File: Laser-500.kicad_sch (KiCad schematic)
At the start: 0 parts

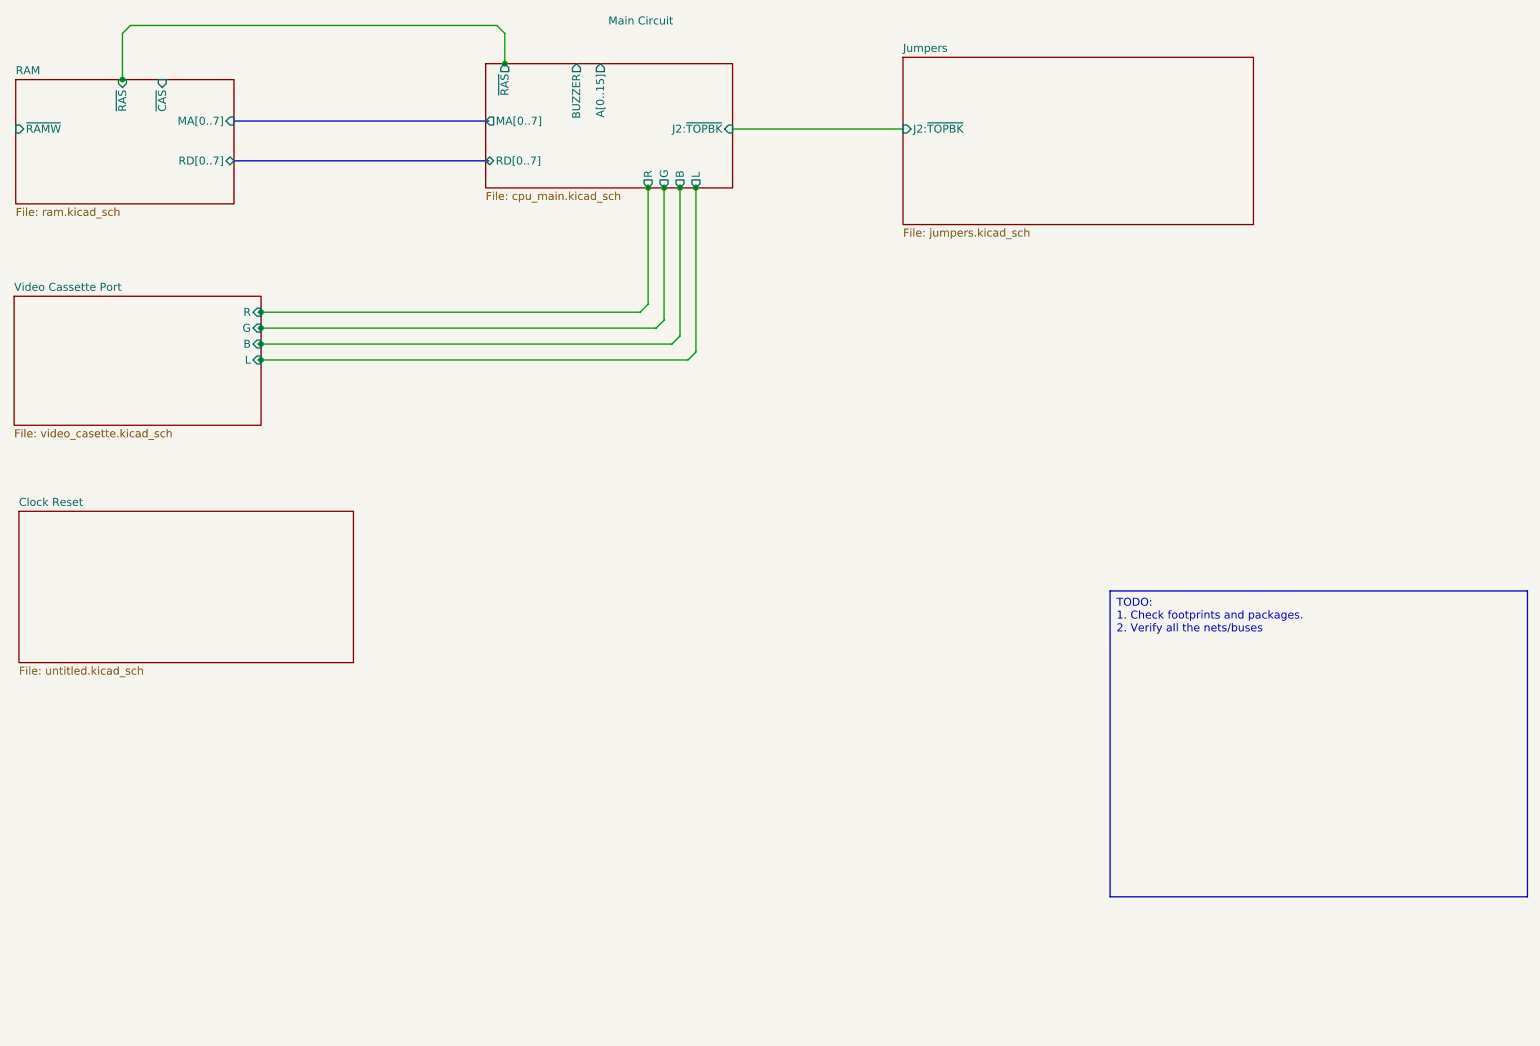
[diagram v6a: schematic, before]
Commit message: More updates on Top and Main diagrams
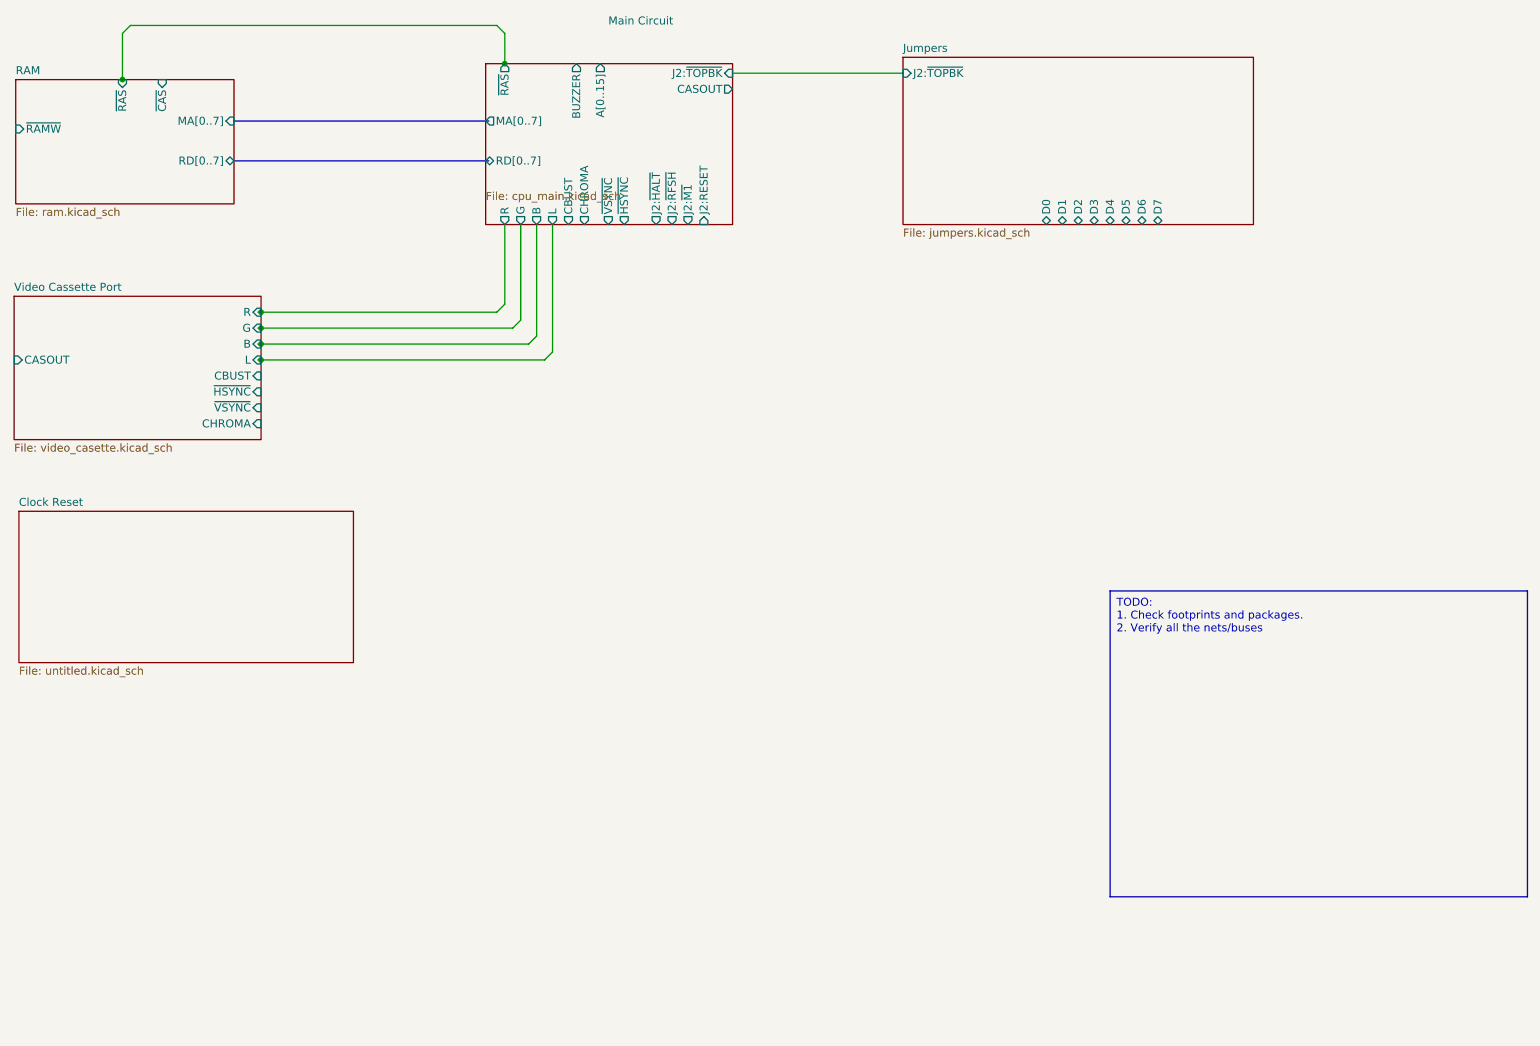
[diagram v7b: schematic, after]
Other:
- sheet Jumpers ports: added D0, D1, D2, D3, D4, D5, D6, D7; removed none
- sheet Main Circuit ports: added CASOUT, CBUST, CHROMA, J2:RESET, J2:~{HALT}, J2:~{M1}, J2:~{RFSH}, ~{HSYNC}, ~{VSYNC}; removed none
- sheet Video Cassette Port ports: added CASOUT, CBUST, CHROMA, ~{HSYNC}, ~{VSYNC}; removed none
